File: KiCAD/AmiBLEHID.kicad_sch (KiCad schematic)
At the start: 7 parts, among them J1 D-Sub Female, SW1 Reset, SW2 Mode, U1 ESP32-H2-Zero, U2 74HC05

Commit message: WIP - Updates for new iteration with WS2812 LEDs
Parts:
- LED1, LED2: footprint LED_SMD:LED_WS2812B_PLCC4_5.0x5.0mm_P3.2mm -> LED_SMD:LED_WS2812B-Mini_PLCC4_3.5x3.5mm
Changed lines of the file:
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@@
 			)
 		)
-		(property "Footprint" "LED_SMD:LED_WS2812B_PLCC4_5.0x5.0mm_P3.2mm"
+		(property "Footprint" "LED_SMD:LED_WS2812B-Mini_PLCC4_3.5x3.5mm"
 			(at 170.18 143.51 0)
 			(effects
@@
 			)
 		)
-		(property "Footprint" "LED_SMD:LED_WS2812B_PLCC4_5.0x5.0mm_P3.2mm"
+		(property "Footprint" "LED_SMD:LED_WS2812B-Mini_PLCC4_3.5x3.5mm"
 			(at 146.05 143.51 0)
 			(effects

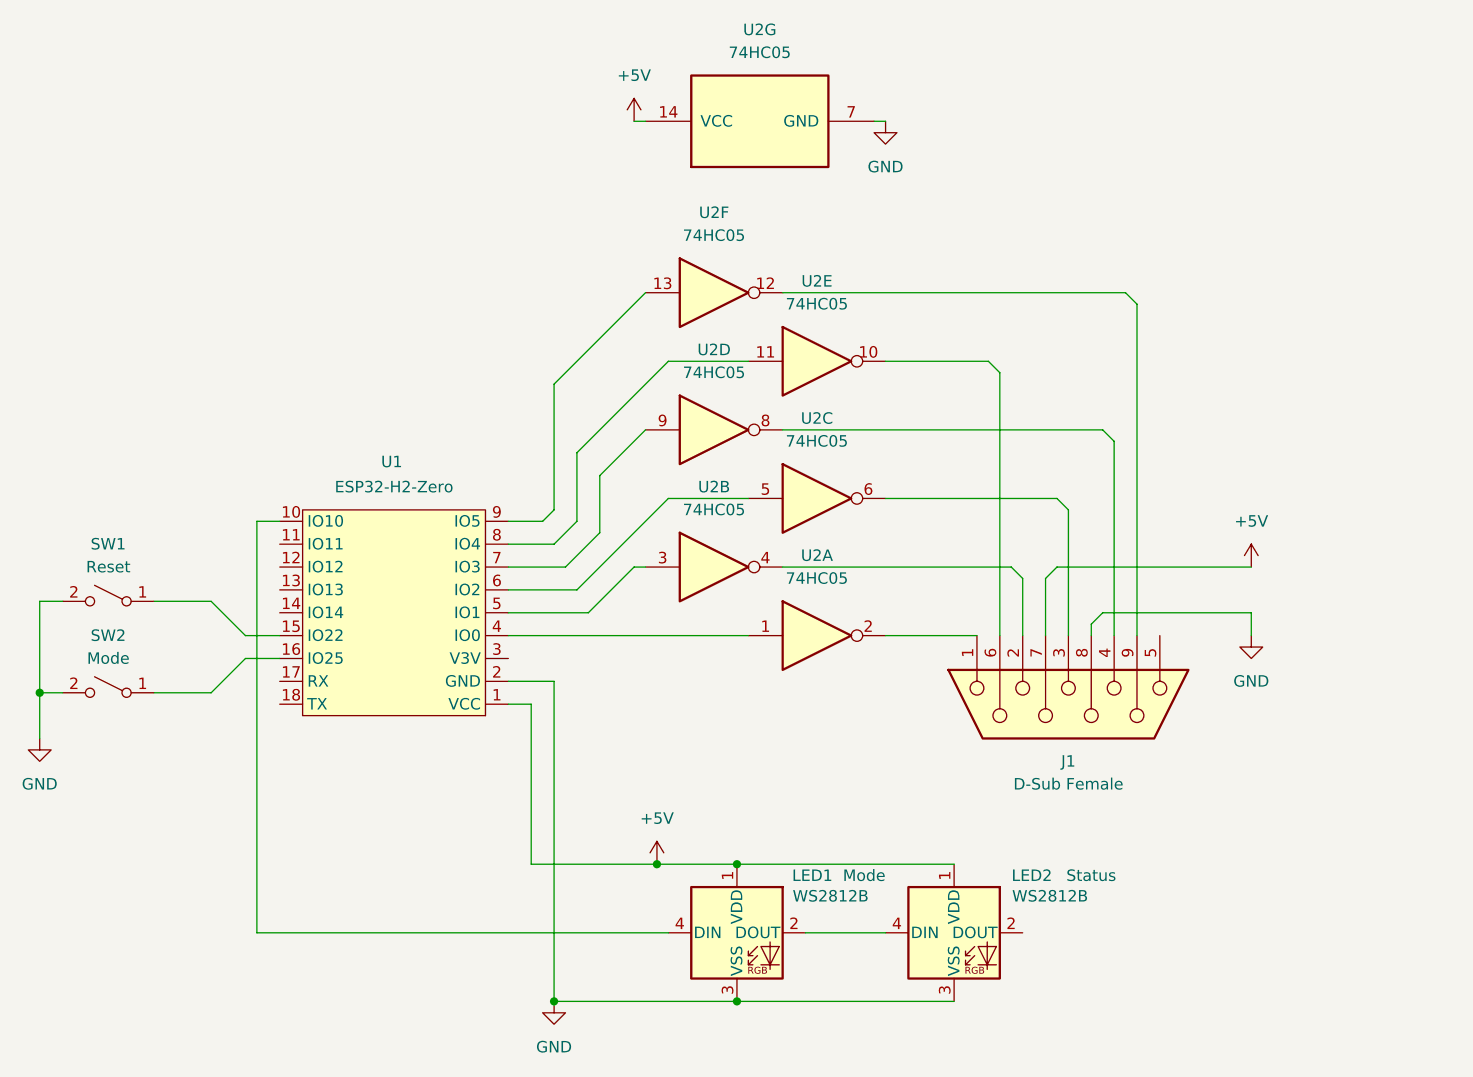
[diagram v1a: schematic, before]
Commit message: KiCAD project updates - *untested* 0.4 revision aimed at enabling CD32 protocol support
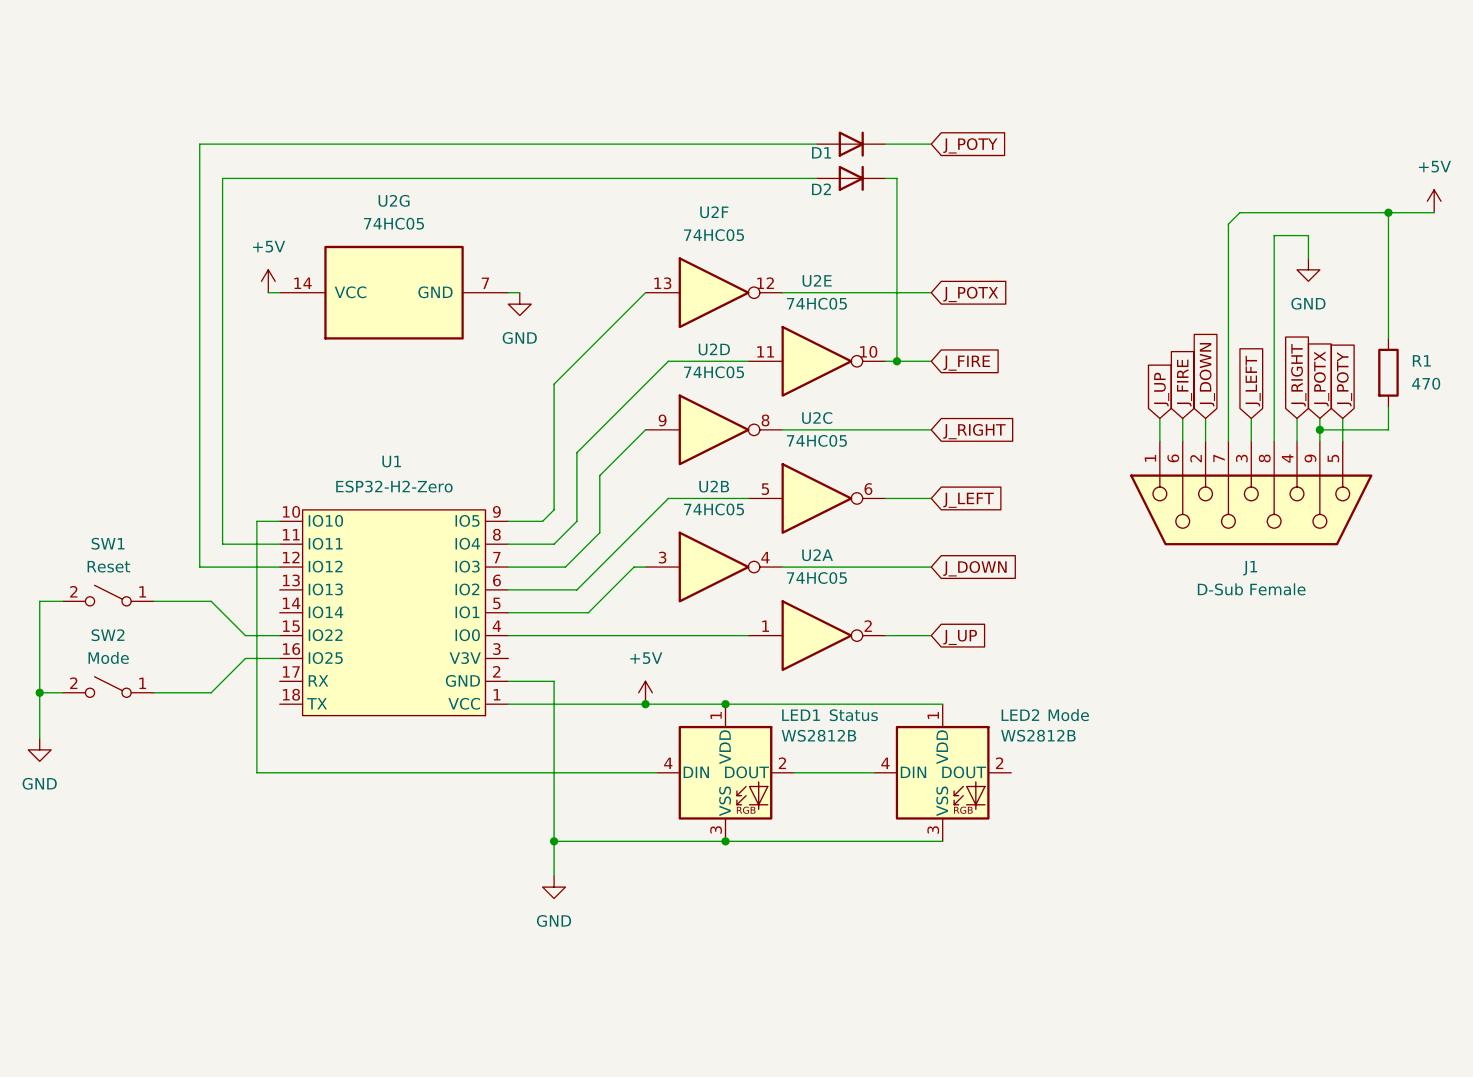
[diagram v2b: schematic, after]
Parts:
- added D1, D2: 1N4148, Diode_SMD:D_1206_3216Metric, symbol Device:D
- added R1: 470, Resistor_SMD:R_1206_3216Metric, symbol Device:R
- LED1: Usage Mode -> Status
- LED2: Usage Status -> Mode
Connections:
- net +5V: now also R1.1
- net J_FIRE: now reaches J1.6, U2.10
- net J_FIRE: now also D2.1 (K)
- net J_POTX: now reaches J1.9, U2.12
- net J_POTX: now also R1.2
- net at U1.11 (IO11): now also D2.2 (A)
- net at U1.12 (IO12): now also D1.2 (A)
- net J_UP: now reaches J1.1, U2.2
- net J_LEFT: now reaches J1.3, U2.6
- net J_RIGHT: now reaches J1.4, U2.8
- net J_DOWN: now reaches J1.2, U2.4
- net J_POTY: now reaches J1.5
- net J_POTY: now also D1.1 (K)
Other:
- moved on the sheet: J1, LED1, LED2, U2G
